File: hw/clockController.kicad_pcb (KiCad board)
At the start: 2 copper layers, 50 x 24 mm, 41 parts, among them J1 TC2030-CTX, J2 JST S02B-PASK, J3 JST S02B-PASK, Q1 IRF7606PBF, SW1 SW_DIP_x01, U1 ISL3295E, U2 ATSAMD11D14A, U3 MCP16301, U4 MAX_M8Q, U5 AB-RTCMC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

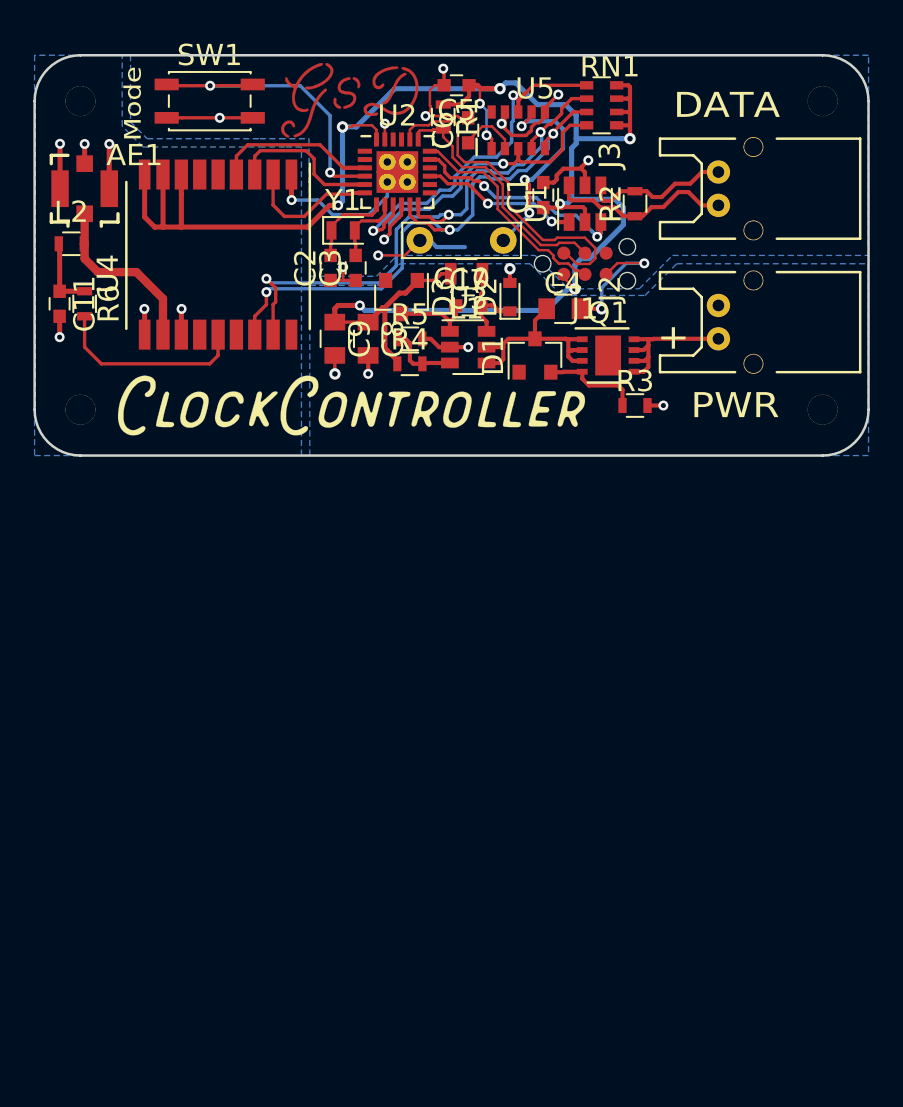
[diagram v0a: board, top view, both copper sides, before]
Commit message: Update kicad project, and samd11 firmware.
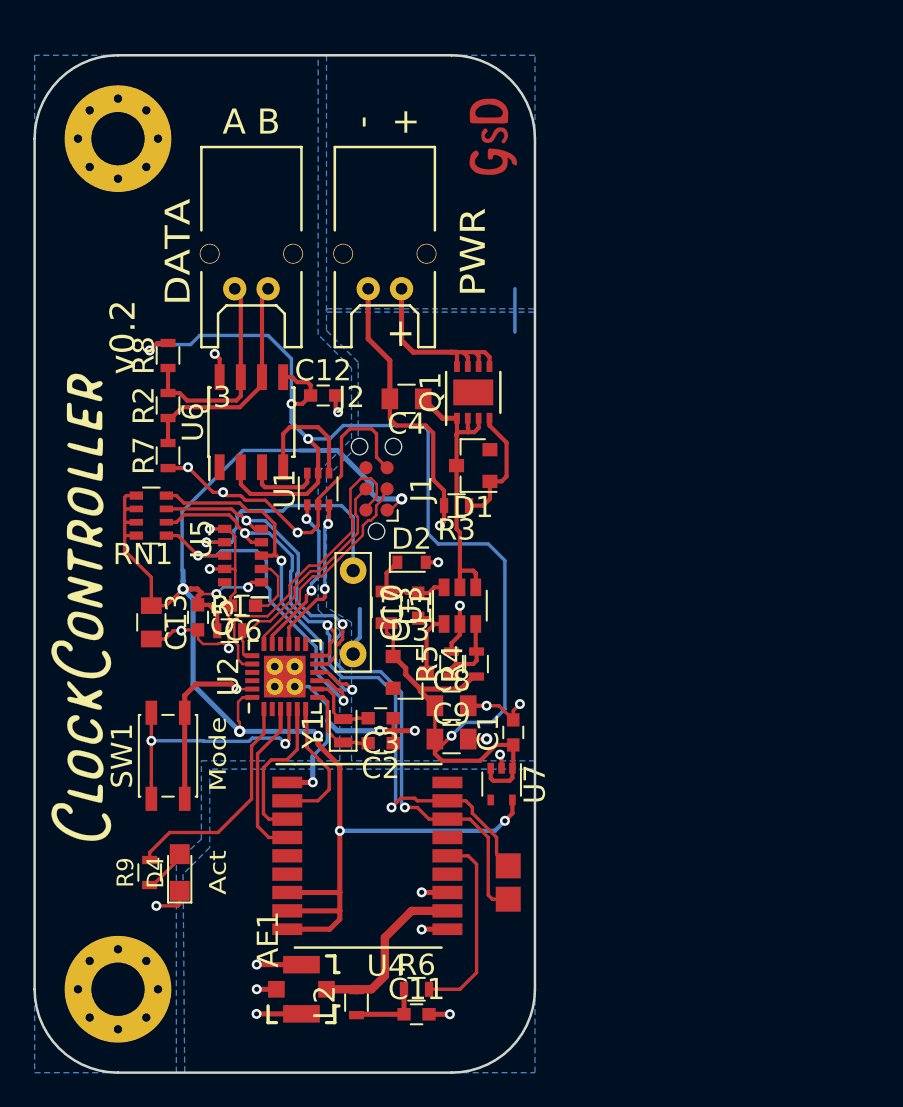
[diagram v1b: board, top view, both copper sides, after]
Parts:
- removed the REF** at (147.2, 102.8)
- removed the REF** at (102.8, 102.8)
- removed the REF** at (102.8, 121.2)
- removed the REF** at (147.2, 121.2)
- added C12: 100n, Capacitors_SMD:C_0603, F.Cu at (117.3, 120.4)
- added C13: 10uF, Capacitors_SMD:C_0805, F.Cu at (107.0, 134.0)
- added D4: LED, LEDs:LED_0805, F.Cu at (108.7, 149.0)
- added R7: 680R, Resistors_SMD:R_0603, F.Cu at (108.0, 124.0)
- added R8: 680R, Resistors_SMD:R_0603, F.Cu at (108.0, 118.0)
- added R9: 680R, Resistors_SMD:R_0603, F.Cu at (106.9, 149.0)
- added REF**: Measurement_Point_Square-SMD-Pad_Small, Measurement_Points:Measurement_Point_Square-SMD-Pad_Small, F.Cu at (128.4, 150.6)
- added REF**: Measurement_Point_Square-SMD-Pad_Small, Measurement_Points:Measurement_Point_Square-SMD-Pad_Small, F.Cu at (128.4, 148.6)
- added REF**: MountingHole_3.2mm_M3_Pad_Via, Mounting_Holes:MountingHole_3.2mm_M3_Pad_Via, F.Cu at (105.0, 156.0)
- added REF**: MountingHole_3.2mm_M3_Pad_Via, Mounting_Holes:MountingHole_3.2mm_M3_Pad_Via, F.Cu at (105.0, 105.0)
- added U6: SN65176B, Housings_SOIC:SOIC-8_3.9x4.9mm_Pitch1.27mm, F.Cu at (113.0, 122.0)
- added U7: MIC5365, TO_SOT_Packages_SMD:SOT-353_SC-70-5, F.Cu at (128.0, 143.7)
- AE1: value Antenna_Shield -> IPX
- C10: value CP1 -> 470mF
- L2: value 4.7nH -> 47nH
- Q1: value IRF7606PBF -> AON7407
- R4: value 31.6K -> 52.3K
- R5: value 10.0K -> 10K
- RN1: value R_Pack04 -> 4.7K
- SW1: value SW_DIP_x01 -> TACT_SW
- U1: value ISL3295E -> SN74LVC2G17; footprint TO_SOT_Packages_SMD:SOT-23-6 -> TO_SOT_Packages_SMD:SOT-363_SC-70-6
- moved AE1 49.7 mm to (116.0, 156.0), turned to 90 degrees
- moved L2 48.6 mm to (119.3, 156.8), turned to 90 degrees
- moved C11 47.7 mm to (122.9, 157.5), turned to 0 degrees
- moved R6 45.7 mm to (122.9, 156.0), turned to 0 degrees
- moved SW1 39.3 mm to (108.0, 142.0), turned to 90 degrees
- moved U4 37.1 mm to (120.0, 148.0), turned to 180 degrees
- moved RN1 36.5 mm to (107.0, 127.6), turned to 180 degrees
- moved C5 35.5 mm to (109.8, 133.7), turned to 270 degrees
- moved R1 33.4 mm to (111.7, 134.5), turned to 0 degrees
- moved C1 32.3 mm to (128.7, 140.6)
- moved C6 31.5 mm to (112.5, 133.0), turned to 180 degrees
- moved U2 31.0 mm to (115.0, 137.2), turned to 90 degrees
- moved R2 30.5 mm to (108.0, 121.0)
- moved U5 30.4 mm to (112.5, 130.0), turned to 90 degrees
- moved Y1 30.0 mm to (118.5, 140.5), turned to 90 degrees
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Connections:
- C1 pad 1: +3V3 -> +5V
- C8 pad 1: +3V3 -> +5V
- C9 pad 1: +3V3 -> +5V
- D3 pad 2: +3V3 -> +5V
- J1 pad 6: (no net) -> Net-(J1-Pad6)
- J3 pad 1: Net-(J3-Pad1) -> /RS485_B
- J3 pad 2: Net-(J3-Pad2) -> /RS485_A
- L1 pad 2: +3V3 -> +5V
- R2 pad 1: Net-(J3-Pad1) -> /RS485_B
- R2 pad 2: Net-(J3-Pad2) -> /RS485_A
- R4 pad 1: +3V3 -> +5V
- U1 pad 1: RS485_DATA -> RS485_EN
- U1 pad 2: +3V3 -> GND
- U1 pad 3: RS485_EN -> RS485_DATA
- U1 pad 4: Net-(J3-Pad2) -> Net-(U1-Pad4)
- U1 pad 5: GND -> +5V
- U1 pad 6: Net-(J3-Pad1) -> Net-(U1-Pad6)
- U2 pad 1: (no net) -> LED_A
- U2 pad 2: (no net) -> Net-(U2-Pad2)
- U4 pad 13: (no net) -> Net-(U4-Pad13)
- U4 pad 15: (no net) -> Net-(U4-Pad15)
- U4 pad 18: (no net) -> Net-(U4-Pad18)
- U4 pad 5: (no net) -> Net-(U4-Pad5)
- U4 pad 6: (no net) -> Net-(U4-Pad6)
- U5 pad 10: (no net) -> Net-(U5-Pad10)
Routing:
- net +5V: track 0.00 -> 84.4 mm, vias 0 -> 4
- net GND: track 66.4 -> 113.3 mm, vias 23 -> 27
- net +3V3: track 110.7 -> 93.0 mm, vias 9 -> 8
- net /RS485_B: track 0.00 -> 13.9 mm
- net LED_A: track 0.00 -> 13.6 mm
- net /RS485_A: track 0.00 -> 12.7 mm
- net Net-(J3-Pad1): track 11.1 -> 0.00 mm
- net I2C_SDA: track 34.2 -> 44.4 mm
- net Net-(J3-Pad2): track 8.90 -> 0.00 mm
- net I2C_SCL: track 34.6 -> 42.3 mm
- net Net-(U1-Pad4): track 0.00 -> 7.28 mm
- net Net-(C4-Pad1): track 13.0 -> 17.6 mm
- net Net-(U1-Pad6): track 0.00 -> 4.50 mm
- net RS485_EN: track 13.6 -> 10.1 mm
- net RTC_INT1: track 19.6 -> 22.8 mm
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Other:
- board size 50 x 24 mm -> 30 x 61 mm
- board text added: "+ -"
- board text added: "A B"
- board text added: "Act"
- board text added: "v0.2"
